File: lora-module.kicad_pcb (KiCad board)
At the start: 4 copper layers, 27.3 x 24.5 mm, 37 parts, among them P1 CONN_01X07, P2 CONN_01X07, Q1 32MHz, U2 SX1276, U5 PE4259

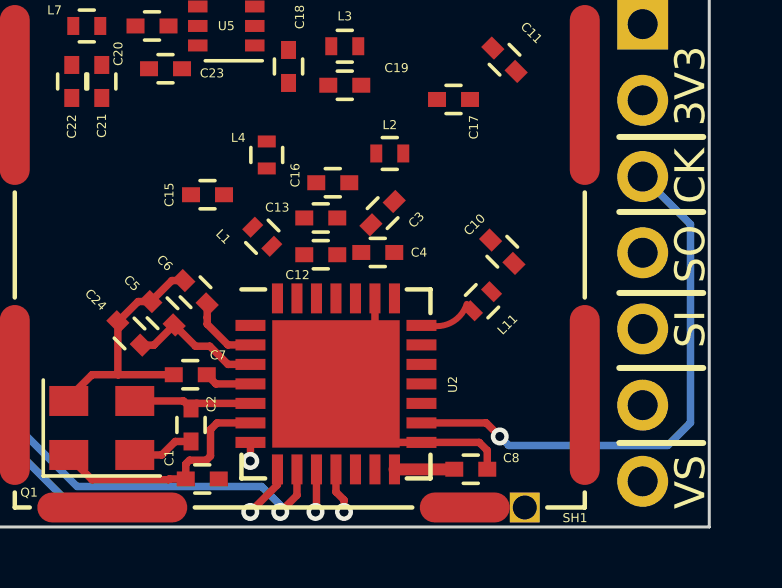
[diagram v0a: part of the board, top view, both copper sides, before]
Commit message: added RF design specification
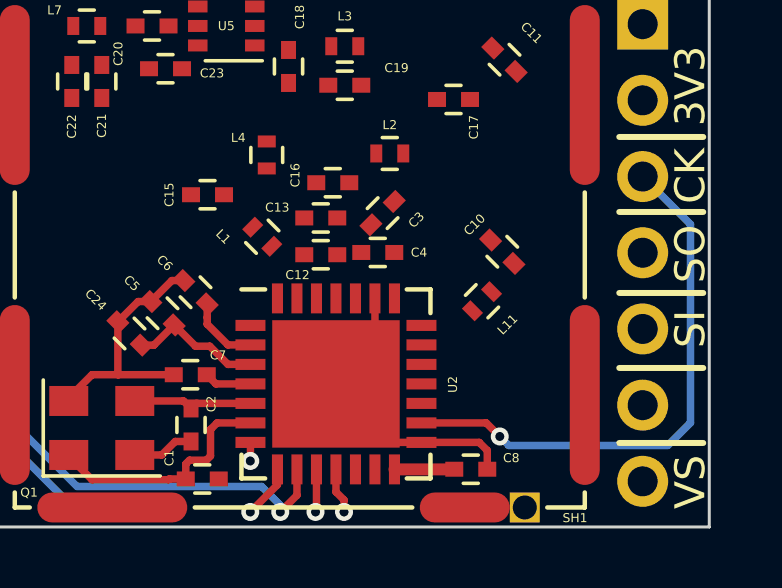
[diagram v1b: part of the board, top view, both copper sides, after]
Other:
- board text added: "50 Ohm line width: Er=4.3 H=0.06858 mm T=0.03556 mm Z0=50.0622Ohm W=0.14 mm S=0.3 mm"
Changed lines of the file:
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@@
     (area 84.949999 87.8 184.100001 118.35)
     (thickness 1.6)
-    (drawings 66)
+    (drawings 67)
     (tracks 122)
     (zones 0)
@@
     )
   )
-  (gr_arc (start 103.215293 107.262355) (end 104.215293 107.562355) (angle 79.64090509) (layer F.Cu) (width 0.2))
-  (gr_text "KIKI PCB 4 layer stack " (at 149 89) (layer Dwgs.User)
-    (effects (font (size 1.5 1.5) (thickness 0.3)))
+  (gr_text "50 Ohm line width: \nEr=4.3\nH=0.06858 mm\nT=0.03556 mm\nZ0=50.0622Ohm\n\nW=0.14 mm\nS=0.3 mm" (at 135 133) (layer Dwgs.User)
+    (effects (font (size 1.5 1.5) (thickness 0.3)) (justify left))
+  )
+  (gr_arc (start 103.215293 107.262355) (end 104.215293 107.562355) (angle 79.6) (layer Dwgs.User) (width 0.13))
+  (gr_text "KIKI PCB 4 layer stack " (at 135 89) (layer Dwgs.User)
+    (effects (font (size 1.5 1.5) (thickness 0.3)) (justify left))
   )
   (gr_text "1.5792 mm" (at 170 117) (layer Dwgs.User)

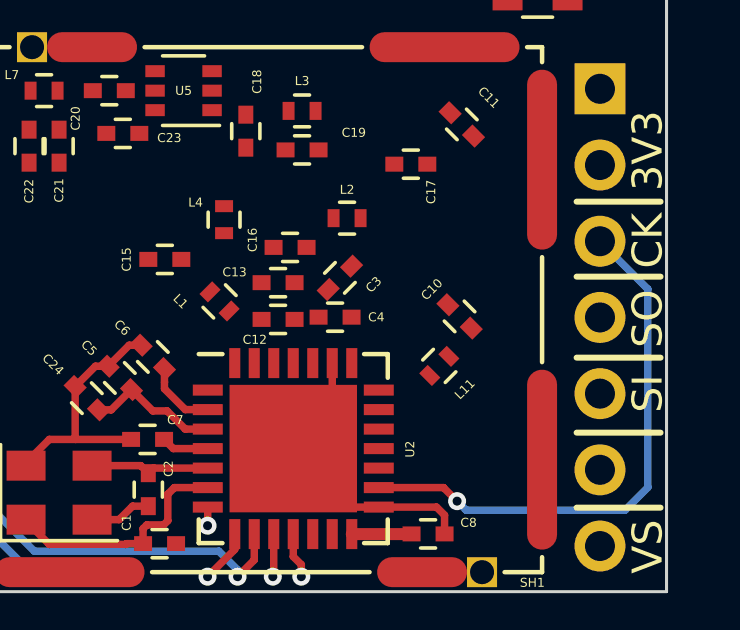
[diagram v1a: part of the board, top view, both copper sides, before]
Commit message: added arcs as RF tracks
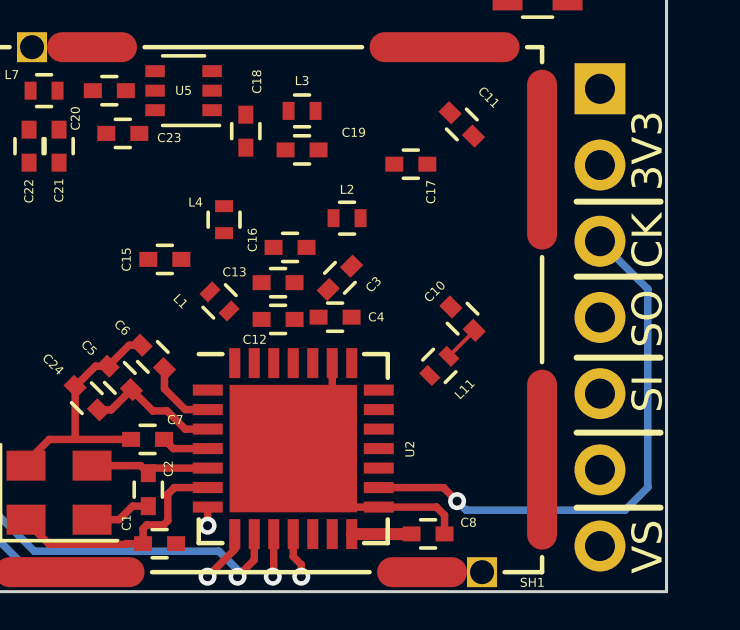
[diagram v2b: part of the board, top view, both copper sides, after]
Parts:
- moved C10 0.12 mm to (105.5, 105.9)
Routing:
- net Net-(C10-Pad1): track 0.00 -> 1.22 mm
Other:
- rule trace_min: 0.2 -> 0.13
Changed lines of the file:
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@@
     (links 102)
     (no_connects 51)
-    (area 84.949999 87.8 184.100001 118.35)
+    (area 84.949999 87.8 184.100001 143.275)
     (thickness 1.6)
-    (drawings 67)
-    (tracks 122)
+    (drawings 69)
+    (tracks 124)
     (zones 0)
     (modules 37)
@@
   )
   (setup
-    (last_trace_width 0.25)
+    (last_trace_width 0.13)
+    (user_trace_width 0.13)
     (user_trace_width 0.4)
     (user_trace_width 0.5)
@@
     (zone_clearance 0.508)
     (zone_45_only no)
-    (trace_min 0.2)
+    (trace_min 0.13)
     (segment_width 0.2)
     (edge_width 0.1)
@@
   )
   (module Capacitors_SMD:C_0402 (layer F.Cu)
-    (at 105.4 105.825 135)
+    (at 105.5 105.9 135)
     (descr "Capacitor SMD 0402, reflow soldering, AVX (see smccp.pdf)")
     (tags "capacitor 0402")
@@
     )
   )
+  (gr_arc (start 99.332742 108.298854) (end 97.2 97.65) (angle 42.54946856) (layer Dwgs.User) (width 0.13))
+  (gr_arc (start 100.420487 103.078938) (end 105.9 99.8) (angle 60.07236586) (layer Dwgs.User) (width 0.13))
   (gr_text "50 Ohm line width: \nEr=4.3\nH=0.06858 mm\nT=0.03556 mm\nZ0=50.0622Ohm\n\nW=0.14 mm\nS=0.3 mm" (at 135 133) (layer Dwgs.User)
     (effects (font (size 1.5 1.5) (thickness 0.3)) (justify left))
   )
-  (gr_arc (start 103.215293 107.262355) (end 104.215293 107.562355) (angle 79.6) (layer Dwgs.User) (width 0.13))
+  (gr_arc (start 103.147889 106.537987) (end 104.35009 107.829879) (angle 46.12026492) (layer Dwgs.User) (width 0.13))
   (gr_text "KIKI PCB 4 layer stack " (at 135 89) (layer Dwgs.User)
     (effects (font (size 1.5 1.5) (thickness 0.3)) (justify left))
@@
   (segment (start 97.00625 110.88125) (end 95.19375 110.88125) (width 0.25) (layer F.Cu) (net 26))
   (segment (start 95.19375 110.88125) (end 95.025 111.05) (width 0.25) (layer F.Cu) (net 26))
+  (segment (start 105.043198 107.156802) (end 105.888909 106.311091) (width 0.13) (layer F.Cu) (net 29))
+  (segment (start 105.888909 106.311091) (end 105.888909 106.288909) (width 0.13) (layer F.Cu) (net 29))
   (zone (net 2) (net_name GND) (layer In1.Cu) (hatch edge 0.508)
     (connect_pads (clearance 0.508))

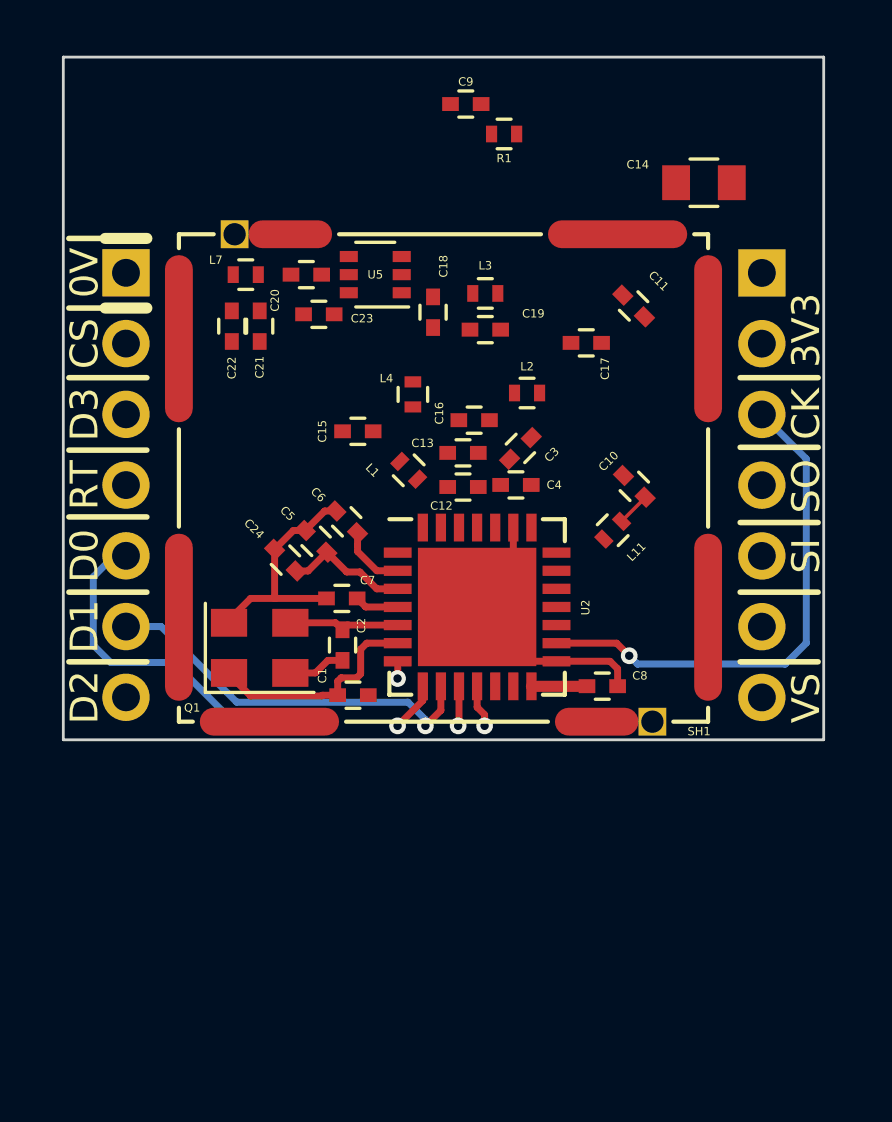
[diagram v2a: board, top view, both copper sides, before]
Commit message: removed 2 caps, added routing
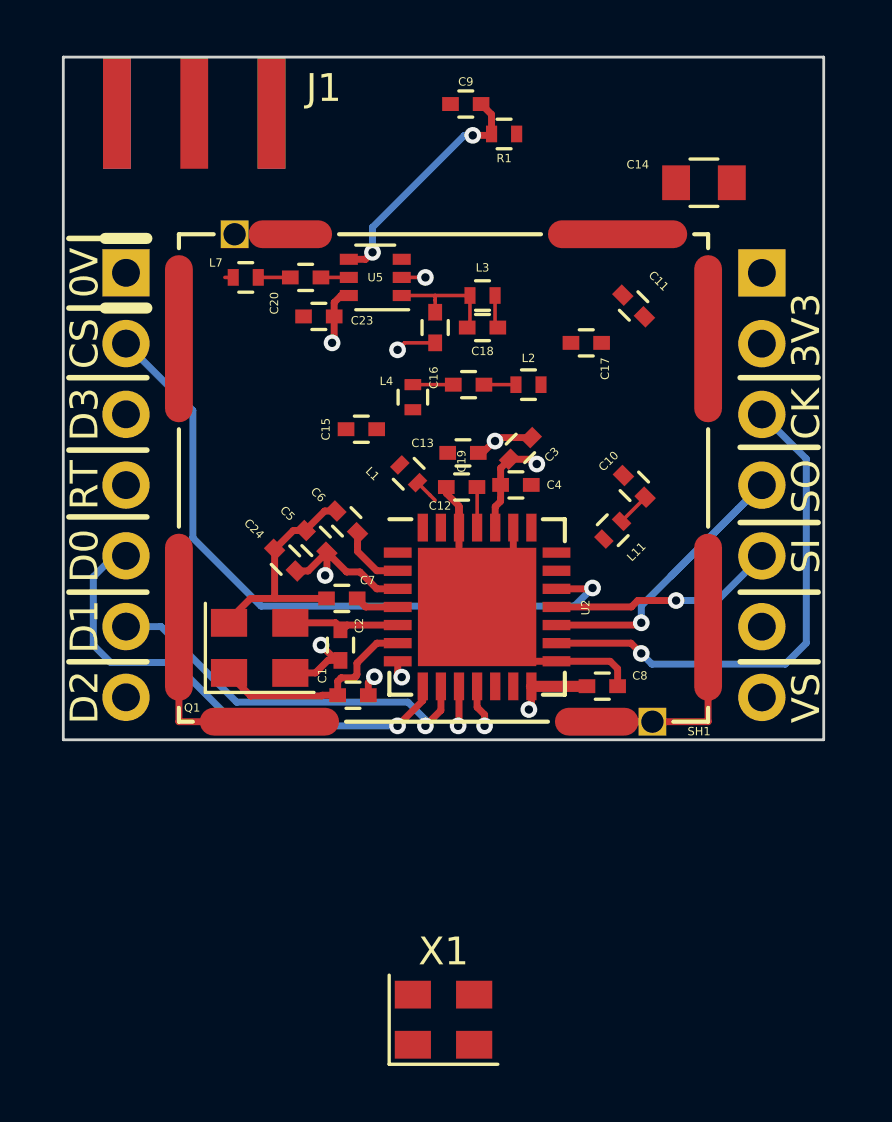
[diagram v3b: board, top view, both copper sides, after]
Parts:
- removed C21, C22: DNP, Capacitors_SMD:C_0402
- added J1: SMA, balcerzak-pcb:SMA-16, F.Cu at (89.7, 92.5)
- added X1: CRYSTAL_SMD, Crystals:Crystal_SMD_EuroQuartz_MT-4pin_3.2x2.5mm, F.Cu at (98.7, 125.1)
- moved C18 1.86 mm to (100.0, 100.2), turned to 0 degrees
- moved C19 1.80 mm to (98.3, 100.2), turned to 90 degrees
- moved C16 1.29 mm to (99.5, 102.2)
- moved L2 0.30 mm to (101.7, 102.2)
- moved C15 0.15 mm to (95.7, 103.8)
- moved L3 0.13 mm to (100.0, 99.0)
- moved L1 0.12 mm to (97.4, 105.5)
- moved C20 0.10 mm to (93.7, 98.4)
- moved L4 0.10 mm to (97.5, 102.7)
- moved L7 0.10 mm to (91.5, 98.4)
- moved U5 0.10 mm to (96.2, 98.4)
- moved C2 0.08 mm to (95.0, 111.6)
- moved C23 0.08 mm to (94.2, 99.8)
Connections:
- SH1 pad 1: Net-(SH1-Pad1) -> GND
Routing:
- net GND: track 40.7 -> 67.2 mm, vias 0 -> 5
- net /CS: track 0.00 -> 24.9 mm, vias 0 -> 1
- net /MISO: track 0.00 -> 14.5 mm, vias 0 -> 1
- net Net-(C9-Pad2): track 0.00 -> 8.75 mm, vias 0 -> 2
- net /MOSI: track 0.00 -> 8.13 mm, vias 0 -> 1
- net +3V3: track 6.46 -> 14.0 mm, vias 0 -> 4
- net /DIO0: track 12.3 -> 18.2 mm
- net Net-(C18-Pad1): track 0.00 -> 4.24 mm
- net Net-(C12-Pad1): track 0.00 -> 1.46 mm
- net Net-(C15-Pad1): track 0.00 -> 1.45 mm
- net Net-(C17-Pad1): track 0.00 -> 1.19 mm
- net Net-(C20-Pad1): track 0.00 -> 1.15 mm
- net Net-(C16-Pad1): track 0.00 -> 1.15 mm
- net Net-(C20-Pad2): track 0.00 -> 1.00 mm
- net Net-(L1-Pad1): track 0.00 -> 0.89 mm
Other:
- net class Default: via_drill 0.4 -> 0.3

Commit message: added all traces and fix top poligon
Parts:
- removed X1: CRYSTAL_SMD, Crystals:Crystal_SMD_EuroQuartz_MT-4pin_3.2x2.5mm
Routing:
- net Net-(R1-Pad2): track 0.00 -> 22.5 mm, vias 0 -> 2
- net +3V3: track 14.0 -> 22.7 mm
- net GND: track 67.2 -> 73.7 mm, vias 5 -> 8
- net (no net): track 0.00 -> 0.14 mm, vias 0 -> 29

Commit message: added 3d packsge for RF switch
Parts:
- U5: footprint TO_SOT_Packages_SMD:SOT-363_SC-70-6 -> balcerzak-pcb:SOT-363_SC-70-6
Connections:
- P2 pad 7: +3V3 -> Net-(P2-Pad7)
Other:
- board text removed: "VS"
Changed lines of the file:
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@@
 (kicad_pcb (version 4) (host pcbnew 4.0.6)
   (general
-    (links 104)
+    (links 103)
     (no_connects 11)
     (area 84.949999 90.439999 112.350001 115.050001)
     (thickness 1.6)
-    (drawings 81)
+    (drawings 80)
     (tracks 279)
     (zones 0)
     (modules 36)
-    (nets 37)
+    (nets 38)
   )
   (page A4)
@@
   )
   (setup
-    (last_trace_width 0.13)
+    (last_trace_width 0.25)
     (user_trace_width 0.13)
     (user_trace_width 0.4)
@@
   (net 35 "Net-(C20-Pad2)")
   (net 36 "Net-(J1-Pad1)")
+  (net 37 "Net-(P2-Pad7)")
   (net_class Default "This is the default net class."
     (clearance 0.2)
@@
     (add_net "Net-(P2-Pad1)")
     (add_net "Net-(P2-Pad6)")
+    (add_net "Net-(P2-Pad7)")
     (add_net "Net-(R1-Pad2)")
     (add_net "Net-(U2-Pad1)")
@@
       (net 4 "Net-(P2-Pad6)"))
     (pad 7 thru_hole oval (at 0 -15.24 180) (size 1.7 1.7) (drill 1) (layers *.Cu *.Mask)
-      (net 1 +3V3))
+      (net 37 "Net-(P2-Pad7)"))
     (model Pin_Headers.3dshapes/Pin_Header_Straight_1x07_Pitch2.54mm.wrl
       (at (xyz 0 -0.3 0))
@@
     )
   )
-  (module TO_SOT_Packages_SMD:SOT-363_SC-70-6 (layer F.Cu)
+  (module Capacitors_SMD:C_0402 (layer F.Cu)
+    (at 94.175 99.8)
+    (descr "Capacitor SMD 0402, reflow soldering, AVX (see smccp.pdf)")
+    (tags "capacitor 0402")
+    (attr smd)
+    (fp_text reference C23 (at 1.55 0.15) (layer F.SilkS)
+      (effects (font (size 0.3 0.3) (thickness 0.075)))
+    )
+    (fp_text value 1nF (at 0 1.27) (layer F.Fab) hide
+      (effects (font (size 1 1) (thickness 0.15)))
+    )
+    (fp_text user %R (at 0 -1.27) (layer F.Fab) hide
+      (effects (font (size 1 1) (thickness 0.15)))
+    )
+    (fp_line (start -0.5 0.25) (end -0.5 -0.25) (layer F.Fab) (width 0.1))
+    (fp_line (start 0.5 0.25) (end -0.5 0.25) (layer F.Fab) (width 0.1))
+    (fp_line (start 0.5 -0.25) (end 0.5 0.25) (layer F.Fab) (width 0.1))
+    (fp_line (start -0.5 -0.25) (end 0.5 -0.25) (layer F.Fab) (width 0.1))
+    (fp_line (start 0.25 -0.47) (end -0.25 -0.47) (layer F.SilkS) (width 0.12))
+    (fp_line (start -0.25 0.47) (end 0.25 0.47) (layer F.SilkS) (width 0.12))
+    (fp_line (start -1 -0.4) (end 1 -0.4) (layer F.CrtYd) (width 0.05))
+    (fp_line (start -1 -0.4) (end -1 0.4) (layer F.CrtYd) (width 0.05))
+    (fp_line (start 1 0.4) (end 1 -0.4) (layer F.CrtYd) (width 0.05))
+    (fp_line (start 1 0.4) (end -1 0.4) (layer F.CrtYd) (width 0.05))
+    (pad 1 smd rect (at -0.55 0) (size 0.6 0.5) (layers F.Cu F.Paste F.Mask)
+      (net 2 GND))
+    (pad 2 smd rect (at 0.55 0) (size 0.6 0.5) (layers F.Cu F.Paste F.Mask)
+      (net 1 +3V3))
+    (model Capacitors_SMD.3dshapes/C_0402.wrl
+      (at (xyz 0 0 0))
+      (scale (xyz 1 1 1))
+      (rotate (xyz 0 0 0))
+    )
+  )
+  (module balcerzak-pcb:SMA-16 (layer F.Cu)
+    (at 89.7 92.5)
+    (fp_text reference J1 (at 4.65 -0.9) (layer F.SilkS)
+      (effects (font (size 1 1) (thickness 0.15)))
+    )
+    (fp_text value SMA (at 0 0) (layer F.Fab)
+      (effects (font (size 1 1) (thickness 0.15)))
+    )
+    (pad 1 smd rect (at 0 0) (size 1 4) (layers F.Cu F.Paste F.Mask)
+      (net 36 "Net-(J1-Pad1)"))
+    (pad 2 smd rect (at 2.775 0) (size 1 4) (layers F.Cu F.Paste F.Mask)
+      (net 2 GND))
+    (pad 2 smd rect (at -2.775 0) (size 1 4) (layers F.Cu F.Paste F.Mask)
+      (net 2 GND))
+    (pad 2 smd rect (at -2.775 0) (size 1 4) (layers B.Cu B.Paste B.Mask)
+      (net 2 GND))
+    (pad 2 smd rect (at 2.775 0) (size 1 4) (layers B.Cu B.Paste B.Mask)
+      (net 2 GND))
+    (model ../../../../../home/bbalcerzak/work/balcerzak-kicad-lib/balcerzak-3d/kicad/connectors/SMA/SMA.wrl
+      (at (xyz 0 0.08 -0.036))
+      (scale (xyz 0.393701 0.393701 0.393701))
+      (rotate (xyz 90 -180 0))
+    )
+  )
+  (module balcerzak-pcb:SOT-363_SC-70-6 (layer F.Cu)
     (at 96.2 98.4 180)
     (descr "SOT-363, SC-70-6")
@@
     (pad 6 smd rect (at 0.95 -0.65 180) (size 0.65 0.4) (layers F.Cu F.Paste F.Mask)
       (net 1 +3V3))
-  )
-  (module Capacitors_SMD:C_0402 (layer F.Cu)
-    (at 94.175 99.8)
-    (descr "Capacitor SMD 0402, reflow soldering, AVX (see smccp.pdf)")
-    (tags "capacitor 0402")
-    (attr smd)
-    (fp_text reference C23 (at 1.55 0.15) (layer F.SilkS)
-      (effects (font (size 0.3 0.3) (thickness 0.075)))
-    )
-    (fp_text value 1nF (at 0 1.27) (layer F.Fab) hide
-      (effects (font (size 1 1) (thickness 0.15)))
-    )
-    (fp_text user %R (at 0 -1.27) (layer F.Fab) hide
-      (effects (font (size 1 1) (thickness 0.15)))
-    )
-    (fp_line (start -0.5 0.25) (end -0.5 -0.25) (layer F.Fab) (width 0.1))
-    (fp_line (start 0.5 0.25) (end -0.5 0.25) (layer F.Fab) (width 0.1))
-    (fp_line (start 0.5 -0.25) (end 0.5 0.25) (layer F.Fab) (width 0.1))
-    (fp_line (start -0.5 -0.25) (end 0.5 -0.25) (layer F.Fab) (width 0.1))
-    (fp_line (start 0.25 -0.47) (end -0.25 -0.47) (layer F.SilkS) (width 0.12))
-    (fp_line (start -0.25 0.47) (end 0.25 0.47) (layer F.SilkS) (width 0.12))
-    (fp_line (start -1 -0.4) (end 1 -0.4) (layer F.CrtYd) (width 0.05))
-    (fp_line (start -1 -0.4) (end -1 0.4) (layer F.CrtYd) (width 0.05))
-    (fp_line (start 1 0.4) (end 1 -0.4) (layer F.CrtYd) (width 0.05))
-    (fp_line (start 1 0.4) (end -1 0.4) (layer F.CrtYd) (width 0.05))
-    (pad 1 smd rect (at -0.55 0) (size 0.6 0.5) (layers F.Cu F.Paste F.Mask)
-      (net 2 GND))
-    (pad 2 smd rect (at 0.55 0) (size 0.6 0.5) (layers F.Cu F.Paste F.Mask)
-      (net 1 +3V3))
-    (model Capacitors_SMD.3dshapes/C_0402.wrl
-      (at (xyz 0 0 0))
-      (scale (xyz 1 1 1))
-      (rotate (xyz 0 0 0))
-    )
-  )
-  (module balcerzak-pcb:SMA-16 (layer F.Cu)
-    (at 89.7 92.5)
-    (fp_text reference J1 (at 4.65 -0.9) (layer F.SilkS)
-      (effects (font (size 1 1) (thickness 0.15)))
-    )
-    (fp_text value SMA (at 0 0) (layer F.Fab)
-      (effects (font (size 1 1) (thickness 0.15)))
-    )
-    (pad 1 smd rect (at 0 0) (size 1 4) (layers F.Cu F.Paste F.Mask)
-      (net 36 "Net-(J1-Pad1)"))
-    (pad 2 smd rect (at 2.775 0) (size 1 4) (layers F.Cu F.Paste F.Mask)
-      (net 2 GND))
-    (pad 2 smd rect (at -2.775 0) (size 1 4) (layers F.Cu F.Paste F.Mask)
-      (net 2 GND))
-    (pad 2 smd rect (at -2.775 0) (size 1 4) (layers B.Cu B.Paste B.Mask)
-      (net 2 GND))
-    (pad 2 smd rect (at 2.775 0) (size 1 4) (layers B.Cu B.Paste B.Mask)
-      (net 2 GND))
-    (model ../../../../../home/bbalcerzak/work/balcerzak-kicad-lib/balcerzak-3d/kicad/connectors/SMA/SMA.wrl
-      (at (xyz 0 0.08 -0.036))
+    (model ../../../../../home/bbalcerzak/work/balcerzak-kicad-lib/balcerzak-3d/kicad/devices/SO70-6.wrl
+      (at (xyz 0 0 0.018))
       (scale (xyz 0.393701 0.393701 0.393701))
-      (rotate (xyz 90 -180 0))
+      (rotate (xyz -90 0 90))
     )
   )
@@
   )
   (gr_text SI (at 111.67 108.4 90) (layer F.SilkS)
-    (effects (font (size 1 1) (thickness 0.2)))
-  )
-  (gr_text VS (at 111.67 113.5 90) (layer F.SilkS)
     (effects (font (size 1 1) (thickness 0.2)))
   )
@@
   (segment (start 101.80625 113.08125) (end 103.79375 113.08125) (width 0.4) (layer F.Cu) (net 1))
   (segment (start 103.79375 113.08125) (end 103.8 113.075) (width 0.4) (layer F.Cu) (net 1))
+  (segment (start 97.15 98.4) (end 98 98.4) (width 0.13) (layer F.Cu) (net 2))
+  (via (at 98 98.4) (size 0.6) (drill 0.3) (layers F.Cu B.Cu) (net 2))
   (segment (start 104.325 100.75) (end 105.2 100.75) (width 0.13) (layer F.Cu) (net 2))
   (segment (start 105.2 100.75) (end 105.85 101.4) (width 0.13) (layer F.Cu) (net 2))
@@
   (segment (start 97.25 100.75) (end 97 101) (width 0.13) (layer F.Cu) (net 2))
   (via (at 97 101) (size 0.6) (drill 0.3) (layers F.Cu B.Cu) (net 2))
-  (segment (start 97.15 98.4) (end 98 98.4) (width 0.13) (layer F.Cu) (net 2))
-  (via (at 98 98.4) (size 0.6) (drill 0.3) (layers F.Cu B.Cu) (net 2))
   (segment (start 104.15 114.35) (end 106.15 114.35) (width 0.25) (layer F.Cu) (net 2))
   (segment (start 89.15 114.35) (end 89.15 110.6) (width 0.25) (layer F.Cu) (net 2))
